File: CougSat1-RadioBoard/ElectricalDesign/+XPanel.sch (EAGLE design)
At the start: 24 parts, among them J1 ADCS Connector, J2 Low Gain +, J3 Low Gain -, J4 Low Gain Coax, J5 GPS Coax, U1 LTC2499

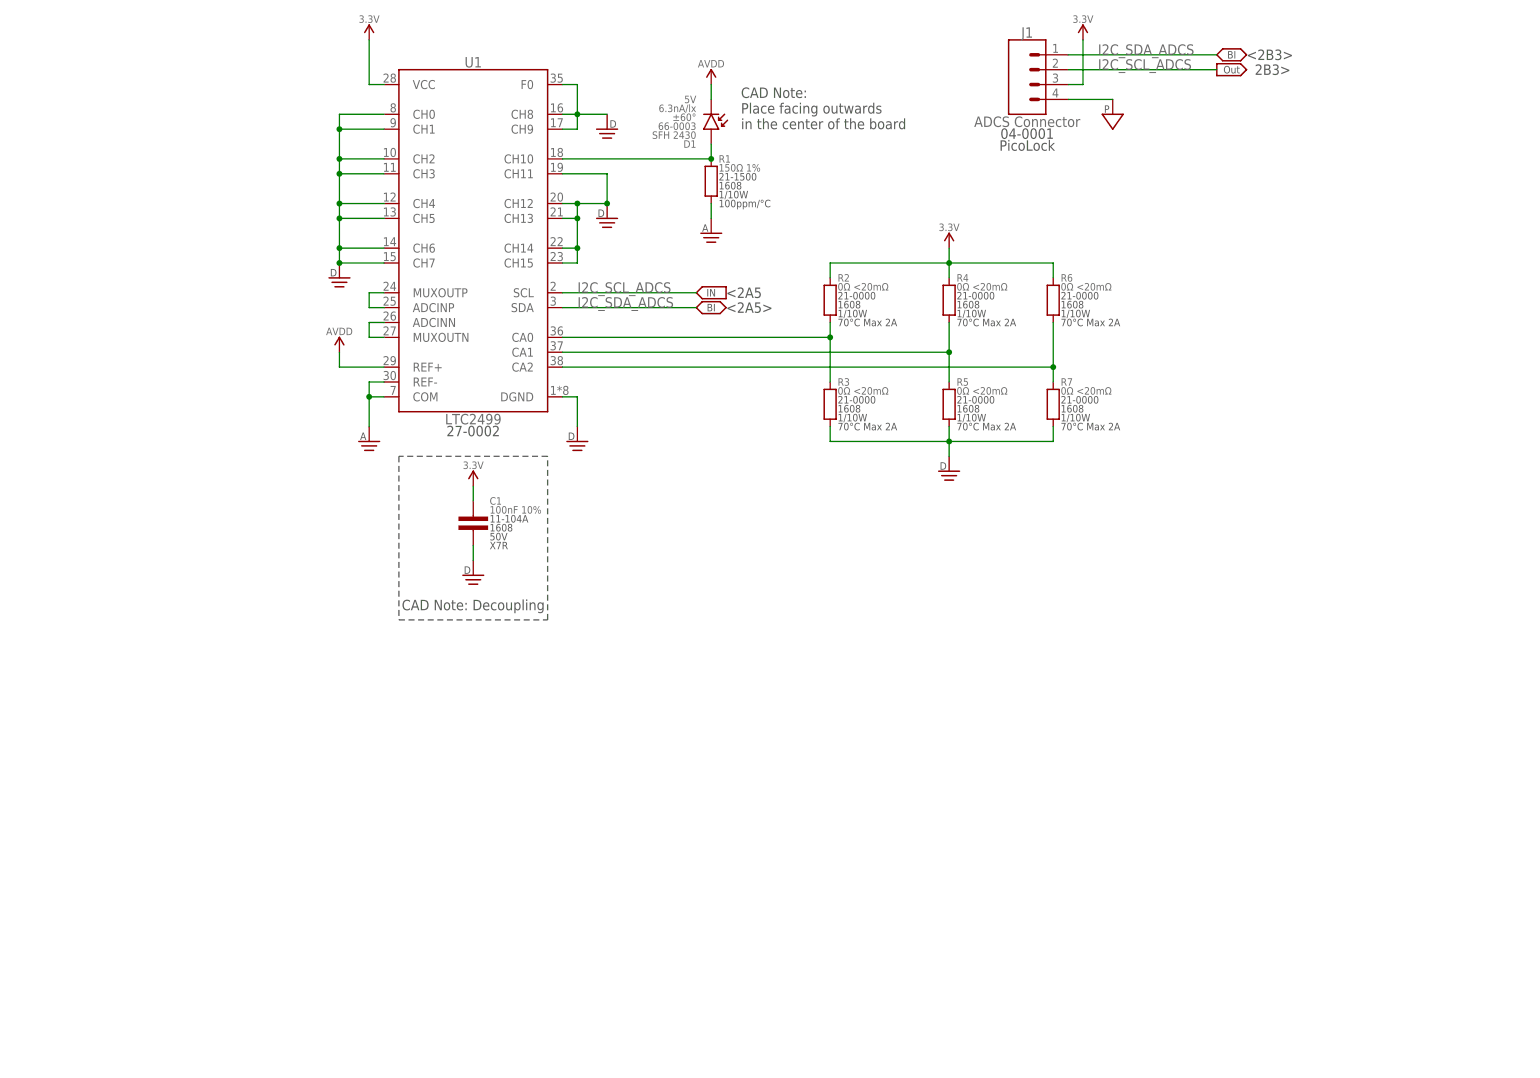
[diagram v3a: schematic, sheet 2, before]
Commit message: Added voltage reference
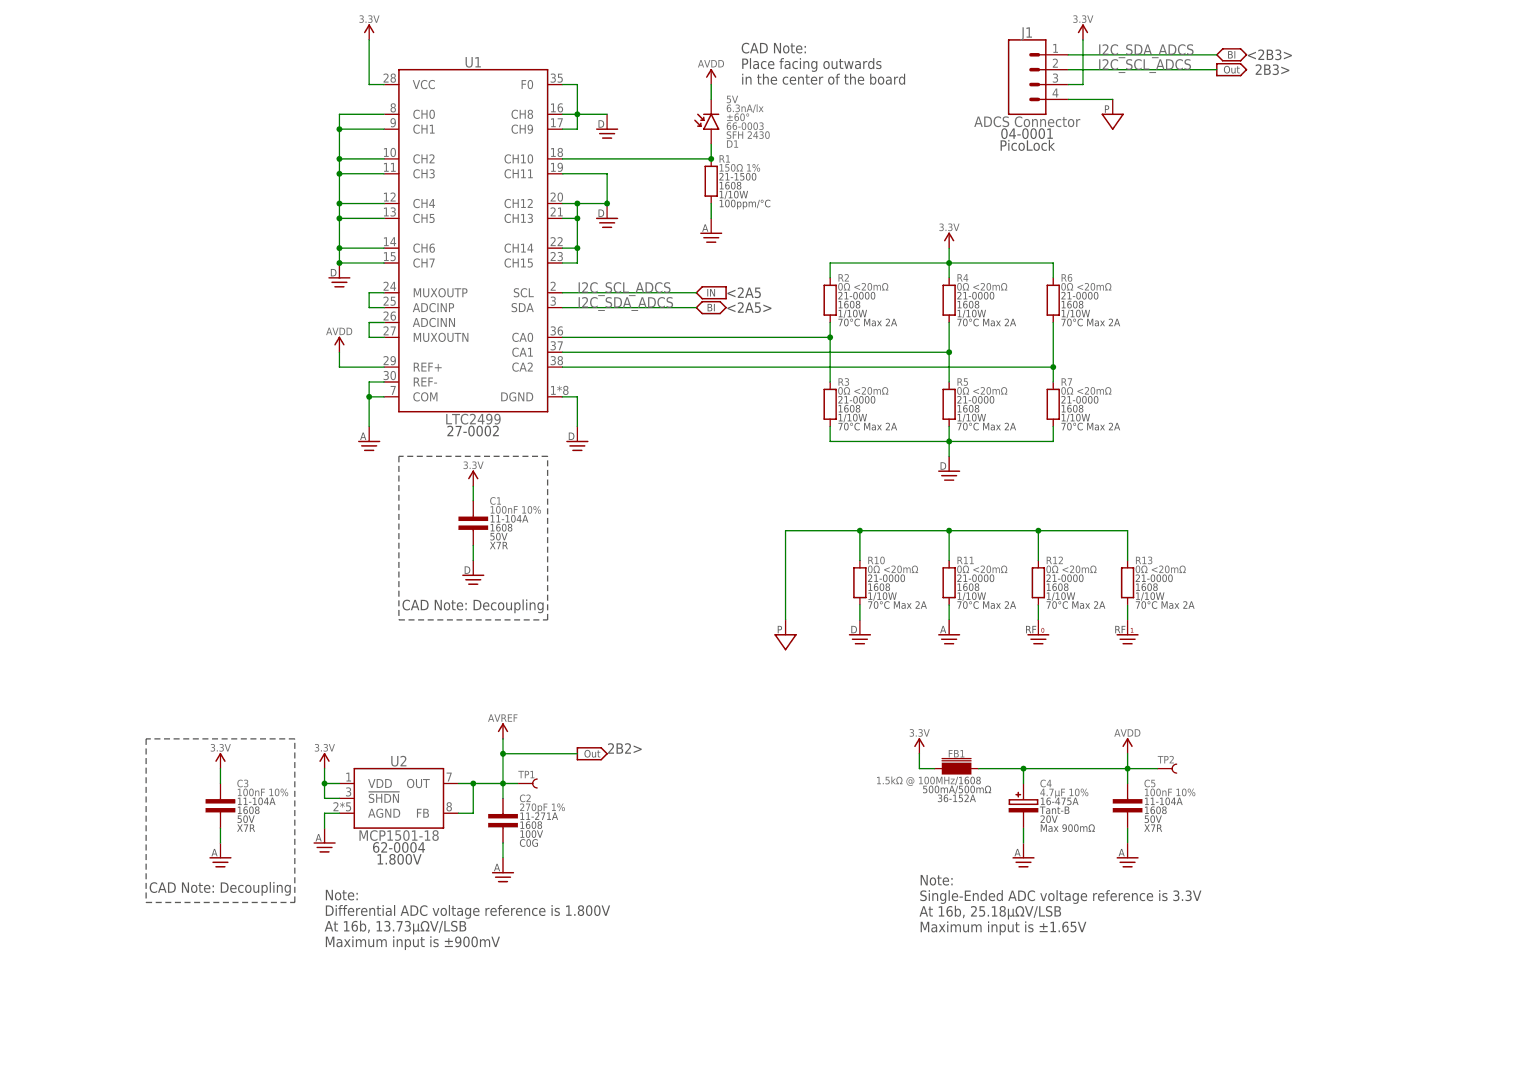
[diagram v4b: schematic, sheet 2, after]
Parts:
- added C2: 270pF 1%, CougsInSpace-Capacitors:CAP-V-270PF-1608
- added C3, C5: 100nF 10%, CougsInSpace-Capacitors:CAP-V-100NF-1608
- added C4: 4.7µF 10%, CougsInSpace-Capacitors:CAP-POL-V-4.7UF-4028
- added FB1: 1.5kΩ @ 100MHz, CougsInSpace-Coils:CHOKE-H-1.5K-1608
- added R10, R11, R12, R13: 0Ω <20mΩ, CougsInSpace-Resistors:RES-V-0-1608
- added TP1, TP2: TEST_POINT-THT-0.7, CougsInSpace-Connectors:TEST_POINT-THT-0.7
- added U2: MCP1501-18, CougsInSpace-IC-Other:MCP1501-18E/RW
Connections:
- net N$1 renamed VCC
- net N$14 renamed PHOTODIODE_SENSE
- net N$2 renamed ADC_IN_N
- net N$3 renamed ADC_IN_P
- net N$5 renamed CA1
- net N$6 renamed CA0
- net N$7 renamed CA2
- new net AVREF: C2.1, TP1.1, U2.FB, U2.OUT
- net 3.3V: now also C3.1, FB1.1, U2.!SHDN, U2.VDD
- net AGND: now also C2.2, C3.2, C4.C, C5.2, R11.1, U2.AGND
- net AVDD: now also C4.A, C5.1, FB1.2, TP2.1
- net DGND: now also R10.1
- net PGND: now also R10.2, R11.2, R12.2, R13.2
- net RFGND-0: now also R12.1
- net RFGND-1: now also R13.1
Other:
- note added: "2B2>"
- note added: "Note: Differential ADC voltage reference is 1.800V At 16b, 13.73µΩV/LSB Maximum input is ±900mV"
- note added: "Note: Single-Ended ADC voltage reference is 3.3V At 16b, 25.18µΩV/LSB Maximum input is ±1.65V"
- moved on the sheet: D1

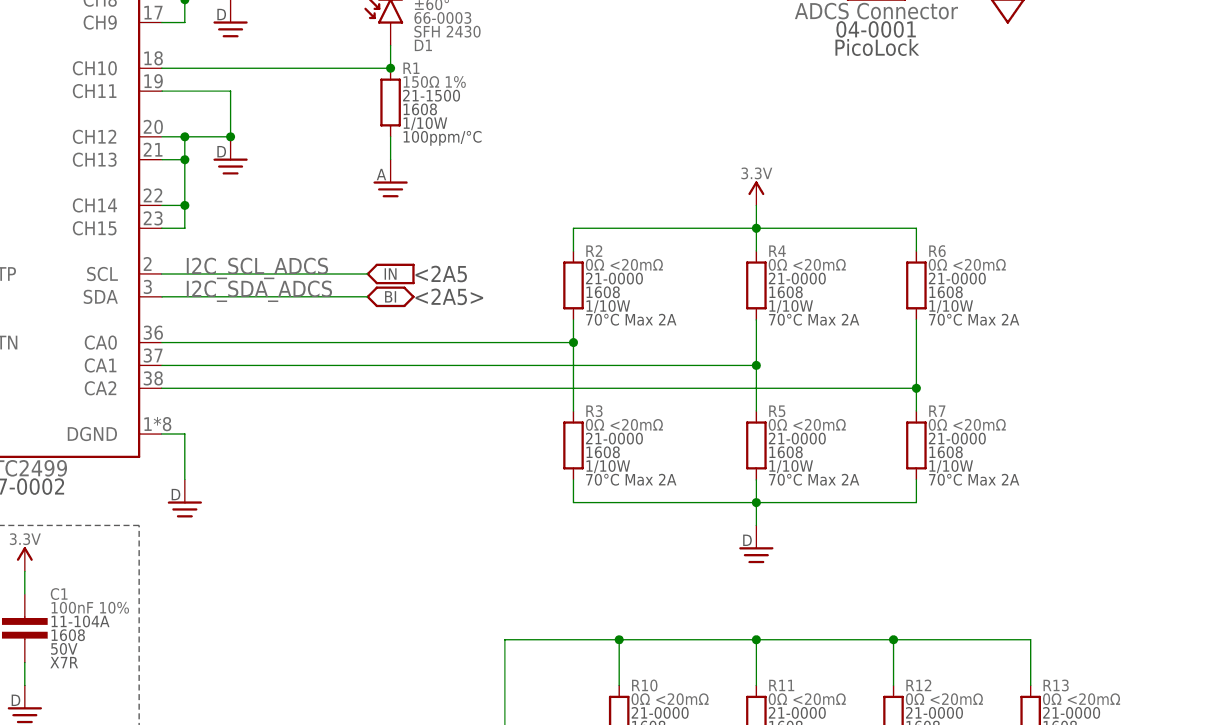
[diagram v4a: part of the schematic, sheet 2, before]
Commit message: Added ADC address
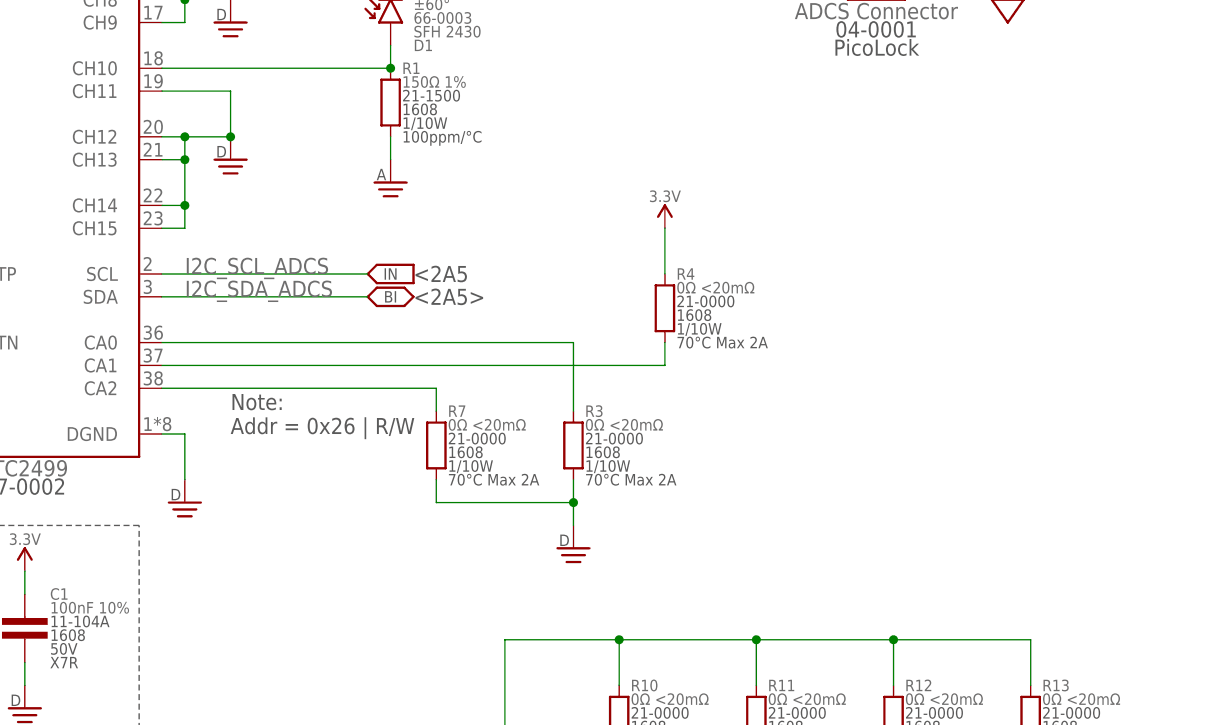
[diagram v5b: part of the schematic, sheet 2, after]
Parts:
- removed R2, R5, R6: 0Ω <20mΩ, CougsInSpace-Resistors:RES-V-0-1608
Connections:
- removed net CA1: R4.1, R5.2, U1.CA1
- removed net CA2: R6.1, R7.2, U1.CA2
- new net N$1: R4.1, U1.CA1
- new net N$2: R7.2, U1.CA2
- net 3.3V: no longer R2.2, R6.2
- net CA0: no longer R2.1
- net DGND: no longer R5.1
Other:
- note added: "Note: Addr = 0x26 | R/W"
- moved on the sheet: R4, R7

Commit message: Updated Document
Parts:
- added H5: M2, CougsInSpace-Hardware:MOUNTING_HOLE-2.2
- J6: value (none) -> Picolock Connector
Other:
- note added: "Note: Differential ADC voltage reference is 1.800V At 16b, 13.73µV/LSB Maximum input is ±900mV"
- note removed: "Note: Differential ADC voltage reference is 1.800V At 16b, 13.73µΩV/LSB Maximum input is ±900mV"
- moved on the sheet: AE1, D1, H1, H2, H3, H4, J5, J6, R8, R9

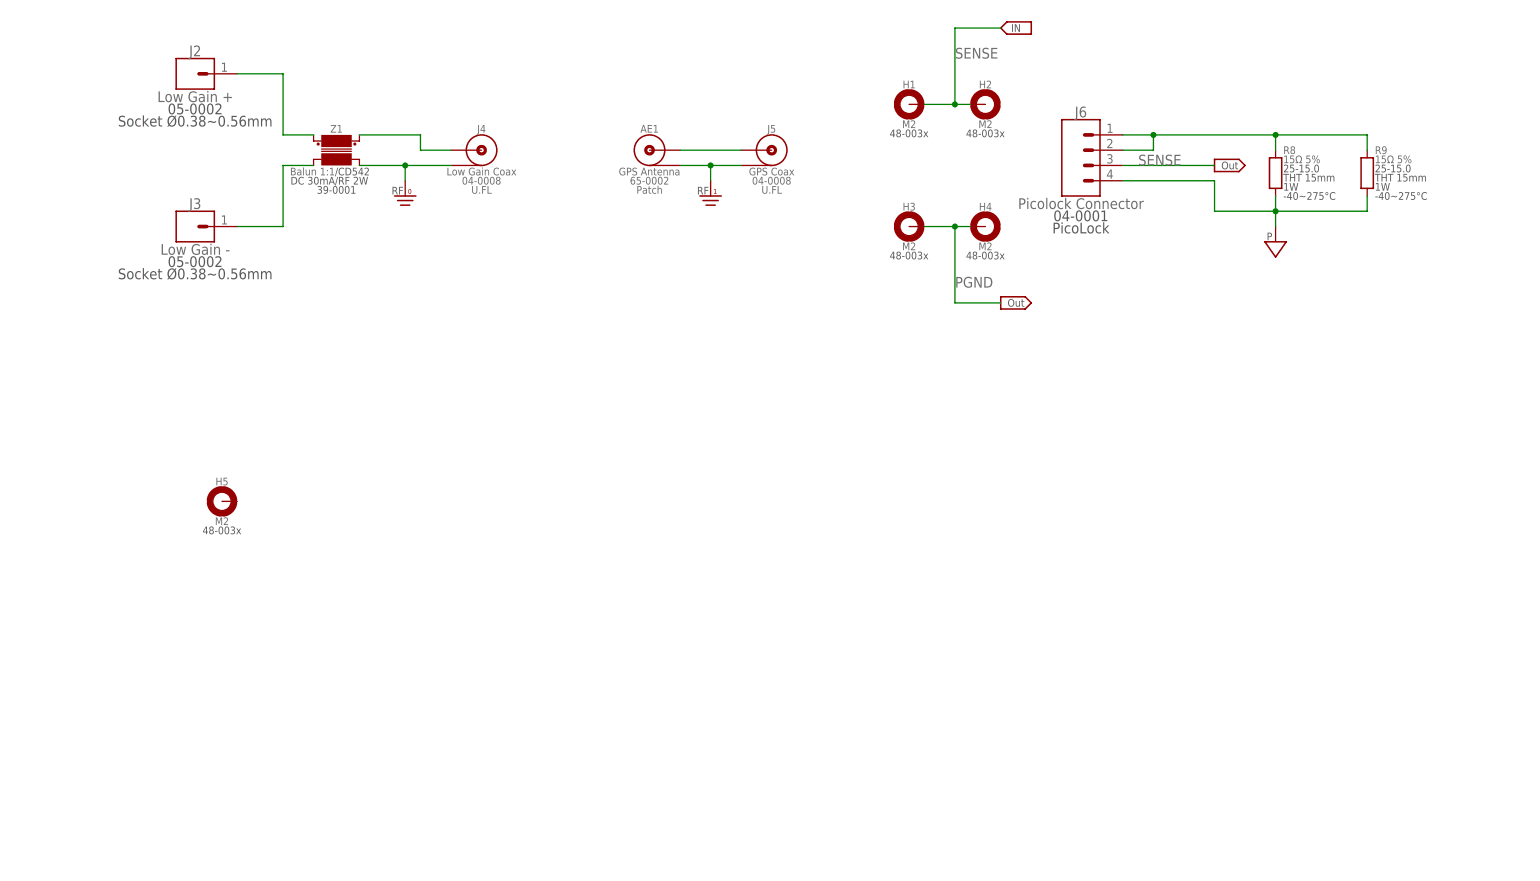
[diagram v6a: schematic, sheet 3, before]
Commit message: Fixed Typo in Document
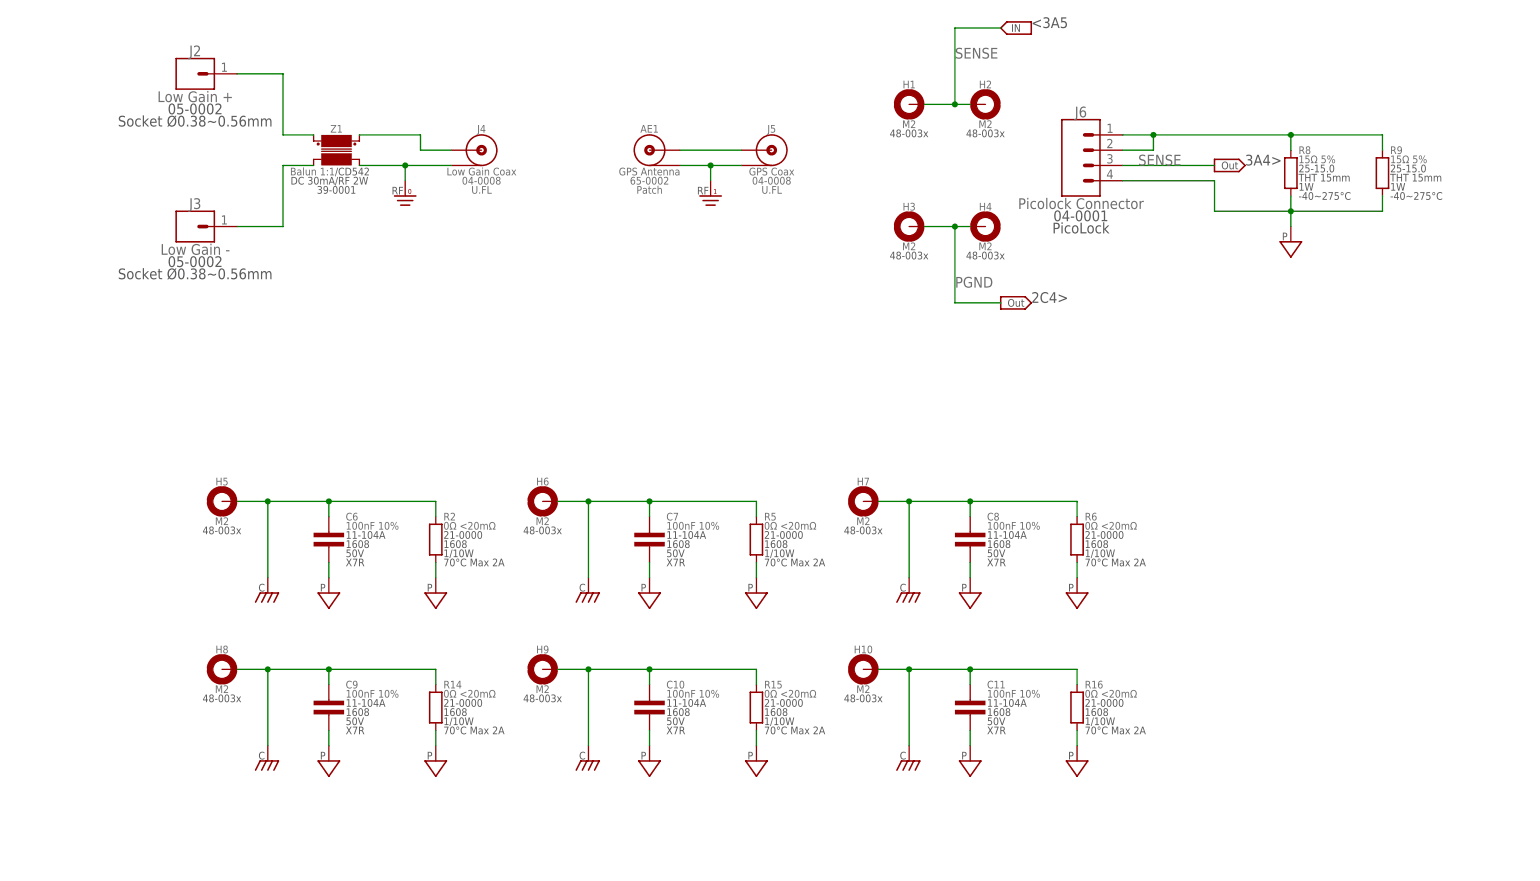
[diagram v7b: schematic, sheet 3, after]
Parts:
- added C10, C11, C6, C7, C8, C9: 100nF 10%, CougsInSpace-Capacitors:CAP-V-100NF-1608
- added H10, H6, H7, H8, H9: M2, CougsInSpace-Hardware:MOUNTING_HOLE-2.2
- added R14, R15, R16, R2, R5, R6: 0Ω <20mΩ, CougsInSpace-Resistors:RES-V-0-1608
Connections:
- net N$1 renamed CA1
- net N$2 renamed CA2
- new net CHASSIS: C10.1, C11.1, C6.1, C7.1, C8.1, C9.1, H10.MOUNT, H5.MOUNT, H6.MOUNT, H7.MOUNT, H8.MOUNT, H9.MOUNT, R14.2, R15.2, R16.2, R2.2, R5.2, R6.2
- net PGND: now also C10.2, C11.2, C6.2, C7.2, C8.2, C9.2, R14.1, R15.1, R16.1, R2.1, R5.1, R6.1
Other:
- note added: "2C4>"
- note added: "3A4>"
- note added: "<3A5"
- moved on the sheet: R8, R9
